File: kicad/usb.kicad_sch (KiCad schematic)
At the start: 5 parts, among them J3 USB_C_Receptacle_USB2.0_14P, U33 CH340N

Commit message: Add caps and make initial placement
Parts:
- added C44: 100n, Capacitor_THT:C_Disc_D5.0mm_W2.5mm_P2.50mm, symbol Device:C
- added C48, C49: 470u, Capacitor_THT:CP_Radial_D10.0mm_P5.00mm, symbol Device:C_Polarized
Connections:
- net GND: now also C44.2, C48.2, C49.2
- net VCC: now also C44.1, C48.1, C49.1

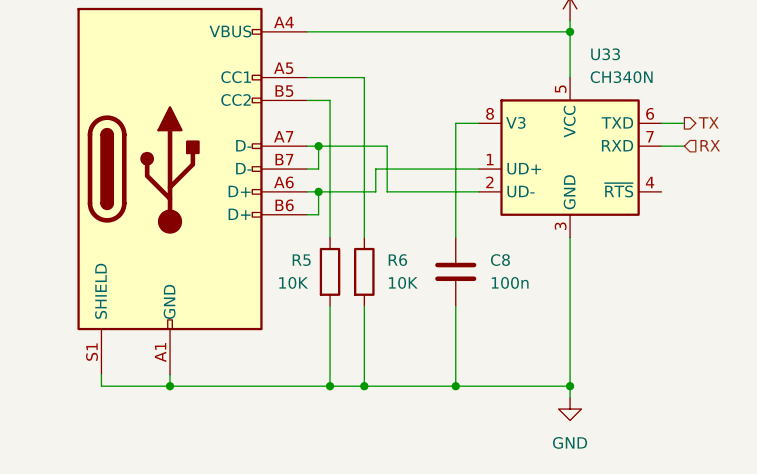
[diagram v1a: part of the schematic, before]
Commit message: hw: Start work on rev B
Changelog:
- fixed IO address decoder (removed /PH2 gating),
- added missing reset circuit capacitor,
- added hardware VGA scrolling,
- removed VGA column register, replaced with address bus,
- fixed values of R5 and R6.
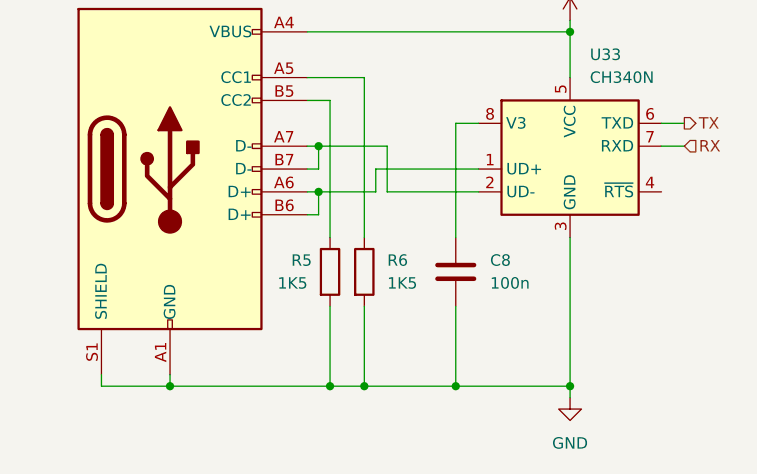
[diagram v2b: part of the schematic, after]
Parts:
- R5, R6: value 10K -> 1K5
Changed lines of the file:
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@@
 			)
 		)
-		(property "Value" "10K"
+		(property "Value" "1K5"
 			(at 130.048 102.87 0)
 			(effects
@@
 			)
 		)
-		(property "Value" "10K"
+		(property "Value" "1K5"
 			(at 142.24 102.8699 0)
 			(effects

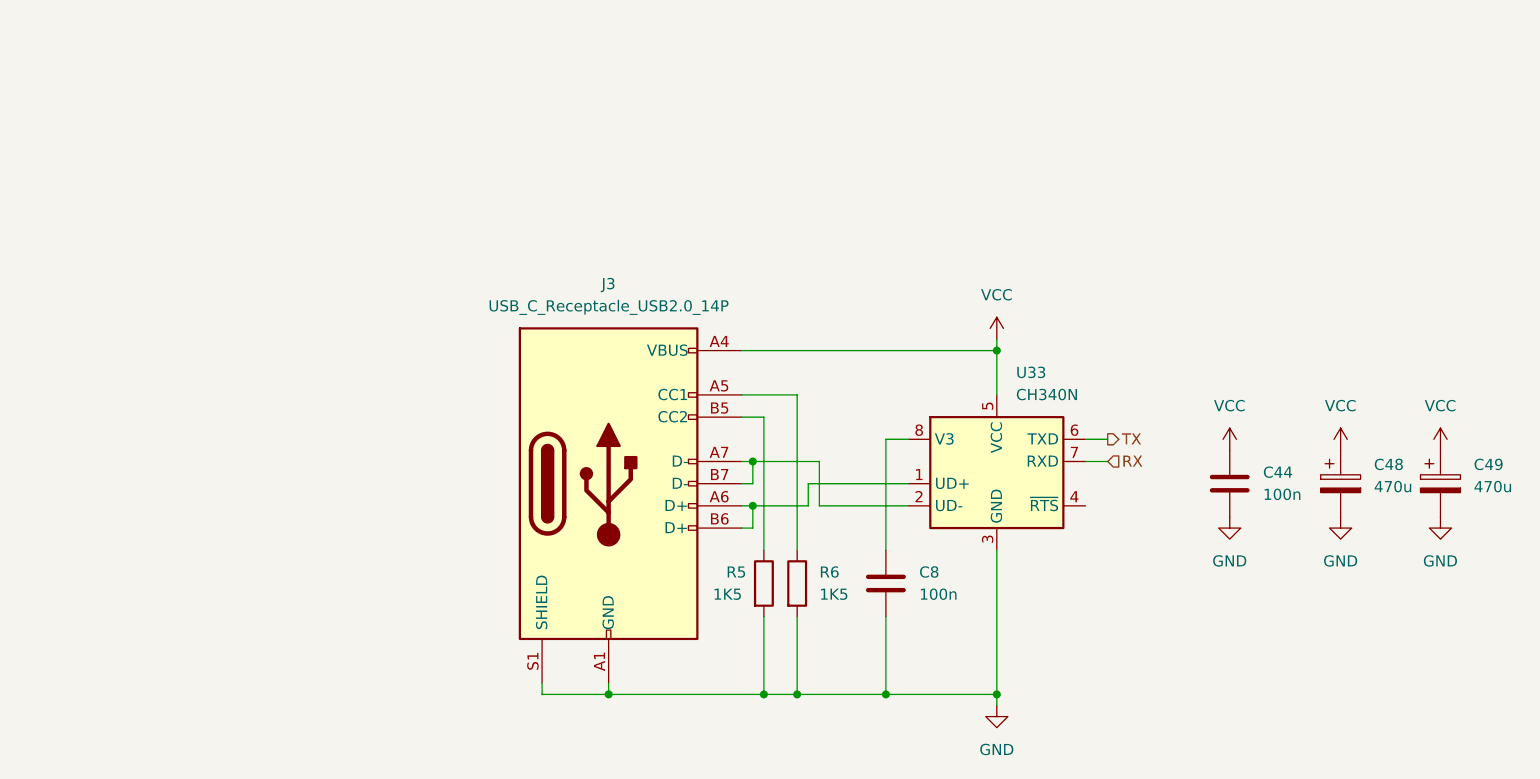
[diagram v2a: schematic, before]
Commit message: hw: revision C
Major changes:
- ROM space has been extended from 16 KiB to 32 KiB
- dynamic RAM option has been removed
- RAM size has been reduced from 32 KiB to 24 KiB
- expansion slot now replaces internal ROM, does not
  have dedicated memory space anymore
- place all I/O within a compactish 8 KiB
- move PH2 gating to /RD and /WR signals
- PCB redo (mechanicaly compatible)
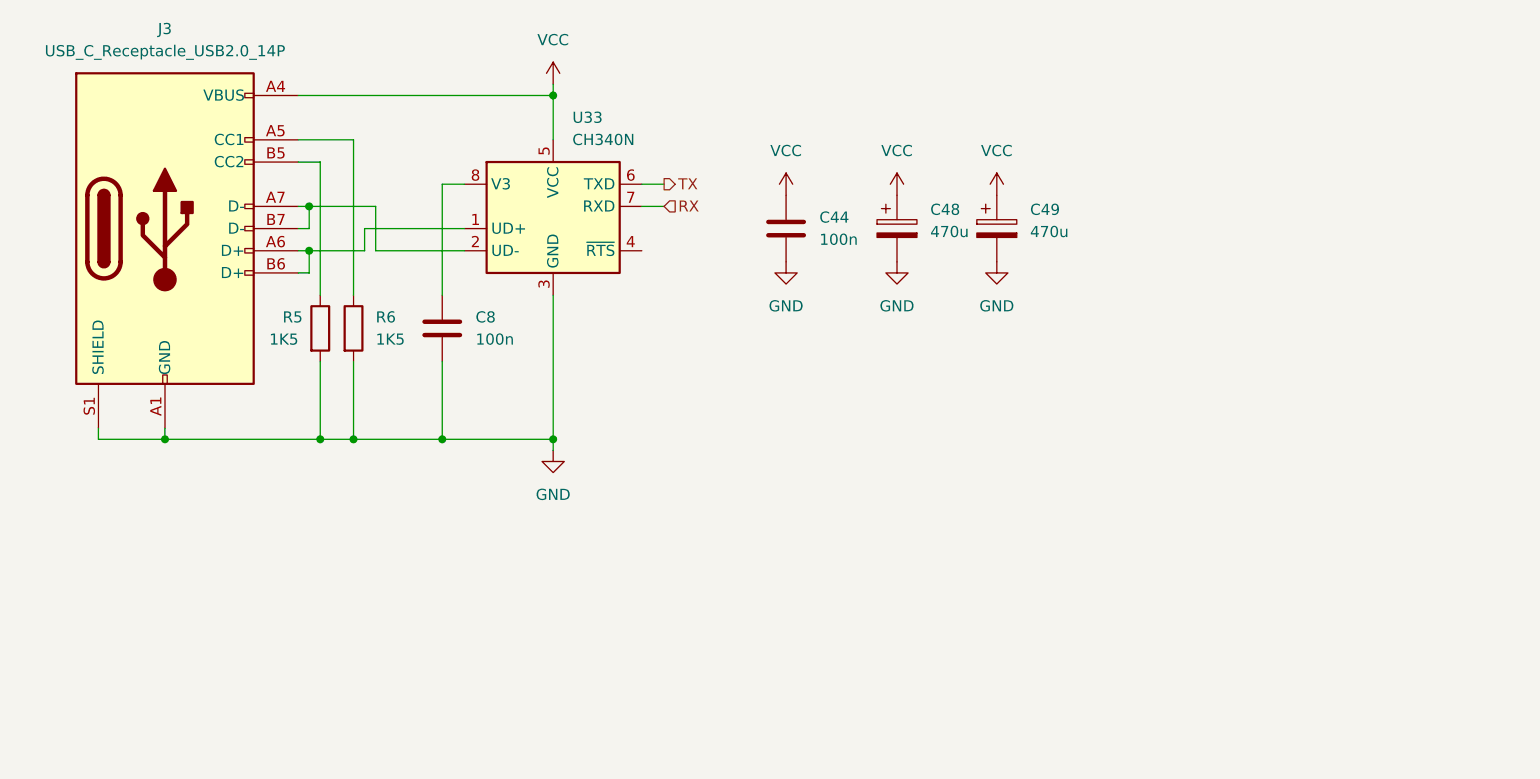
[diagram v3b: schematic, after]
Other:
- moved on the sheet: C44, C48, C49, C8, J3, R5, R6, U33

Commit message: hw: rev D - replace DB25 connector footprint with available one
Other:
- company: (none) -> A.K.
- title: (none) -> USB connector and power
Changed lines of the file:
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@@
 (kicad_sch
-	(version 20231120)
+	(version 20250114)
 	(generator "eeschema")
-	(generator_version "8.0")
+	(generator_version "9.0")
 	(paper "A5")
+	(title_block
+		(title "USB connector and power")
+		(date "2025-08-04")
+		(rev "D")
+		(company "A.K.")
+	)
 	(junction
 		(at 85.09 85.09)
